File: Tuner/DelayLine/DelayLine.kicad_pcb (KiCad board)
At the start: 2 copper layers, 100 x 100 mm, 87 parts, among them J1 Conn_Coaxial, J10 Conn_Coaxial, J11 Conn_Coaxial, J12 Conn_Coaxial, J13 Conn_01x01, J14 Conn_01x01, J15 Conn_01x01, J16 Conn_01x01, J17 Conn_02x10_Odd_Even, J18 Conn_Coaxial, J19 Conn_Coaxial, J2 Conn_01x01, J20 Conn_Coaxial, J21 Conn_Coaxial, J22 Conn_Coaxial, J23 Conn_Coaxial, J24 Conn_01x01, J25 Conn_01x01, J26 Conn_01x01, J27 Conn_01x01, J28 Conn_01x01, J29 Conn_Coaxial, J3 Conn_Coaxial, J31 Conn_Coaxial, J32 Conn_01x01, J33 Conn_01x01, J34 Conn_01x01, J35 Conn_01x01, J5 Conn_Coaxial, J6 Conn_Coaxial, J7 Conn_Coaxial, J8 Conn_01x02, J9 Conn_01x02

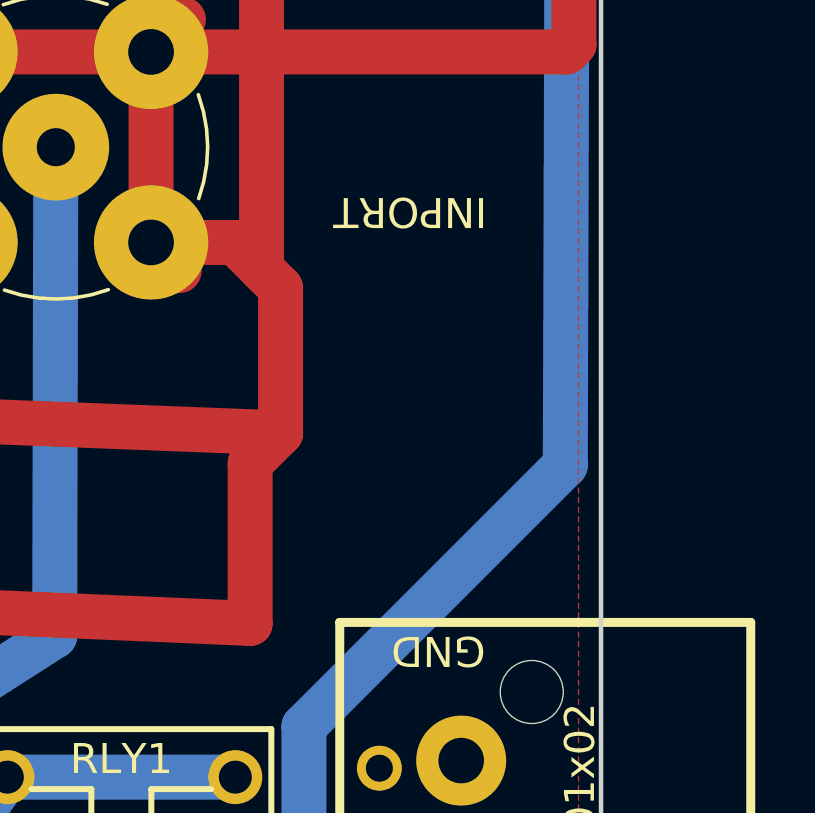
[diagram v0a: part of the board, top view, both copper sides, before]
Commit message: Changed over yet more to BNC
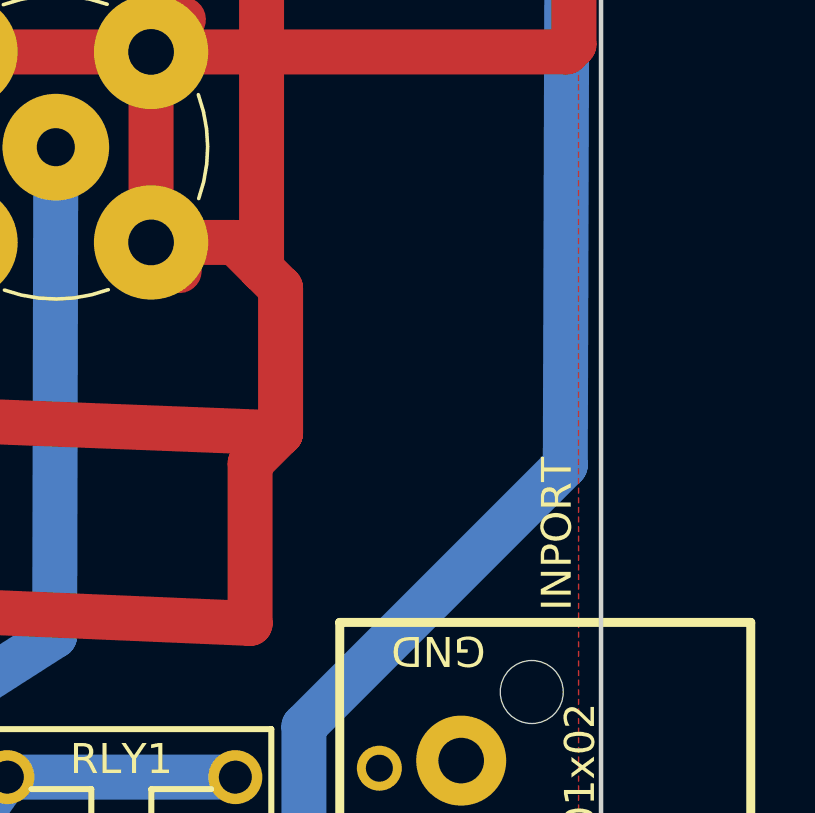
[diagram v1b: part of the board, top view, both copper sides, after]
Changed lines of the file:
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@@
     (links 227)
     (no_connects 0)
-    (area 49.924999 49.924999 150.075001 150.075001)
+    (area 44.941618 47.69538 155.4408 151.075)
     (thickness 1.6)
     (drawings 35)
@@
   )
   (setup
-    (last_trace_width 1.5)
+    (last_trace_width 0.25)
     (user_trace_width 0.35)
     (user_trace_width 0.5)
@@
     (effects (font (size 1 1) (thickness 0.15)))
   )
-  (gr_text INPORT (at 143.637 108.966 180) (layer F.SilkS)
+  (gr_text INPORT (at 148.52904 119.69496 90) (layer F.SilkS)
     (effects (font (size 1 1) (thickness 0.15)))
   )
@@
   (segment (start 137.8104 132.8852) (end 138.35124 132.8852) (width 1.5) (layer B.Cu) (net 62))
   (segment (start 138.35124 132.8852) (end 140.09624 131.1402) (width 1.5) (layer B.Cu) (net 62))
-  (segment (start 148.9202 81.5848) (end 146.51736 78.92796) (width 1.5) (layer B.Cu) (net 62) (status 800020))
+  (segment (start 148.9202 81.5848) (end 146.51736 78.92796) (width 1.5) (layer B.Cu) (net 62) (status 20))
   (segment (start 148.80844 117.40388) (end 148.9202 81.5848) (width 1.5) (layer B.Cu) (net 62))
   (segment (start 140.09624 126.11608) (end 148.80844 117.40388) (width 1.5) (layer B.Cu) (net 62))

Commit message: A few tweaks
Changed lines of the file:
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@@
   (segment (start 137.8104 67.1144) (end 137.9398 67.1144) (width 1.5) (layer B.Cu) (net 52) (status 30))
   (segment (start 124.9072 137.8128) (end 125.7757 137.8128) (width 1.5) (layer B.Cu) (net 53) (status 30))
-  (segment (start 125.7757 137.8128) (end 128.27 136.017) (width 1.5) (layer B.Cu) (net 53) (status 10))
-  (segment (start 128.27 130.533) (end 130.2104 127.8052) (width 1.5) (layer B.Cu) (net 53) (status 20))
-  (segment (start 128.27 136.017) (end 128.27 130.533) (width 1.5) (layer B.Cu) (net 53))
+  (segment (start 125.7757 137.8128) (end 127.5715 135.89) (width 1.5) (layer B.Cu) (net 53) (status 10))
+  (segment (start 127.5715 130.406) (end 130.2104 127.8052) (width 1.5) (layer B.Cu) (net 53) (status 800020))
+  (segment (start 127.5715 135.89) (end 127.5715 130.406) (width 1.5) (layer B.Cu) (net 53))
   (segment (start 124.9072 137.8128) (end 124.9072 138.1533) (width 1.5) (layer F.Cu) (net 53) (status 30))
   (segment (start 137.8104 127.8052) (end 130.2104 127.8052) (width 1.5) (layer B.Cu) (net 53) (status 30))

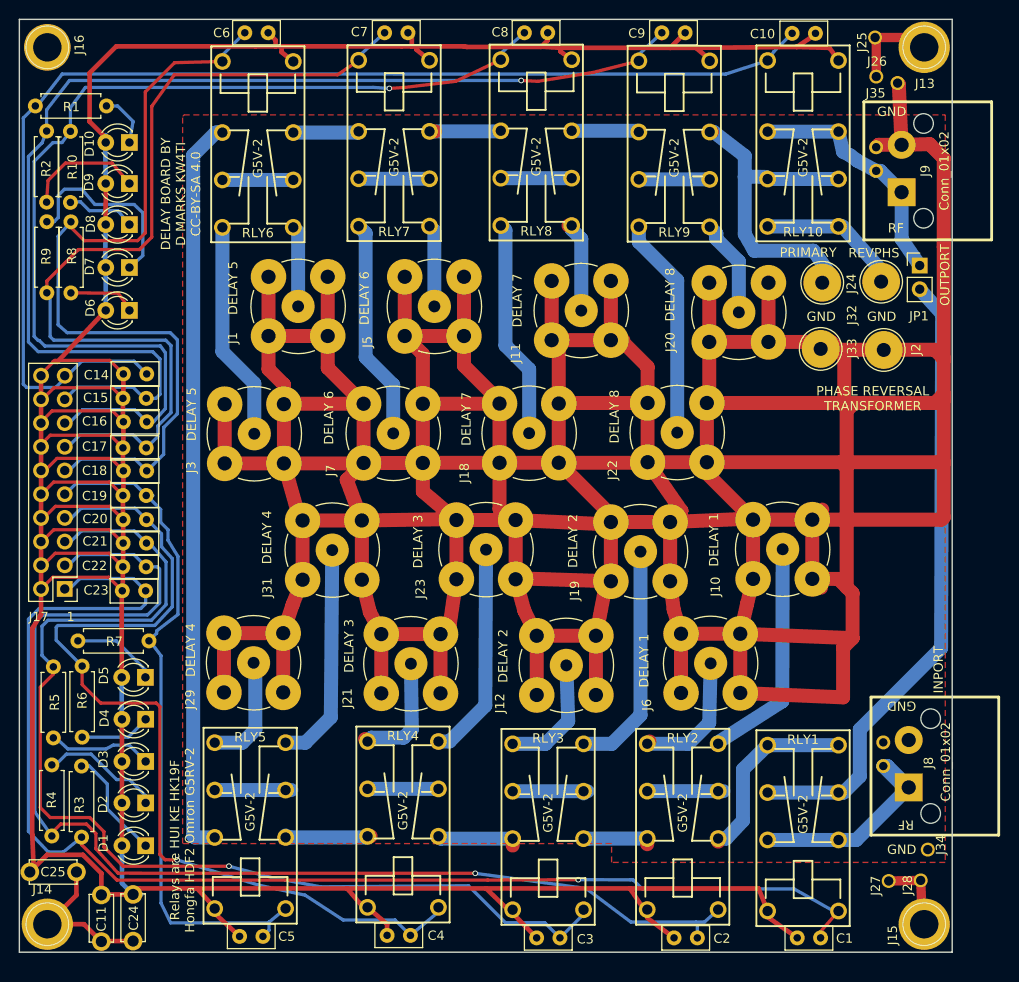
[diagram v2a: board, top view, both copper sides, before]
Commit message: Changed bypass method on delay lines
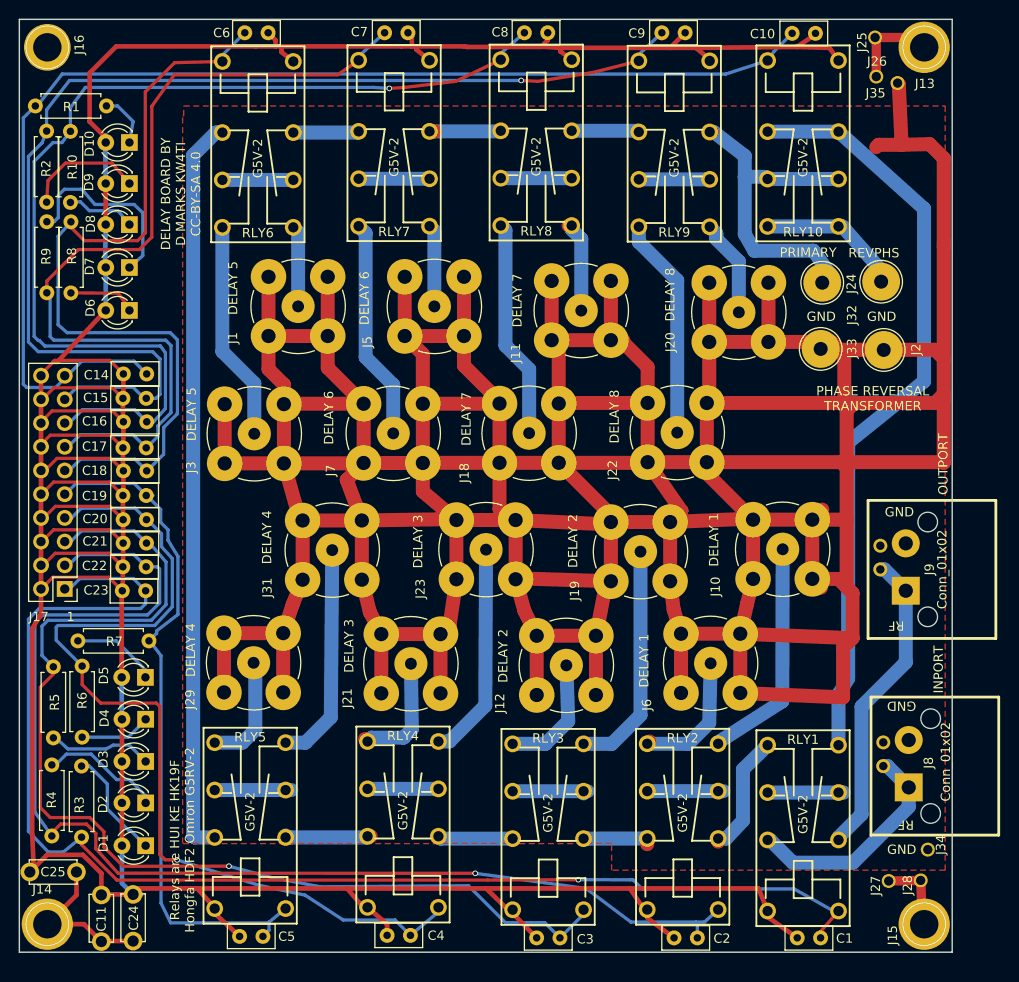
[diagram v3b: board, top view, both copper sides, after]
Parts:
- removed JP1: Jumper_NC_Small, Pin_Headers:Pin_Header_Straight_1x02_Pitch2.54mm
- moved J9 42.7 mm to (154.7, 109.0)
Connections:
- RLY1 pad 6: RFSIG -> RFOUT
- RLY1 pad 8: Net-(RLY1-Pad4) -> RFTHRU
- RLY10 pad 2: RFOUT -> RFTHRU
- RLY10 pad 6: RFOUT -> RFTHRU
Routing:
- net RFTHRU: track 0.00 -> 81.6 mm
- net Net-(RLY1-Pad3): track 67.8 -> 8.70 mm
- net RFGND: track 783.3 -> 766.7 mm
- net Net-(RLY1-Pad4): track 20.6 -> 13.0 mm
- net RFOUT: track 26.1 -> 33.4 mm
- net Net-(RLY3-Pad2): track 8.95 -> 8.21 mm

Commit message: Fixed icom tuning bad tuning report
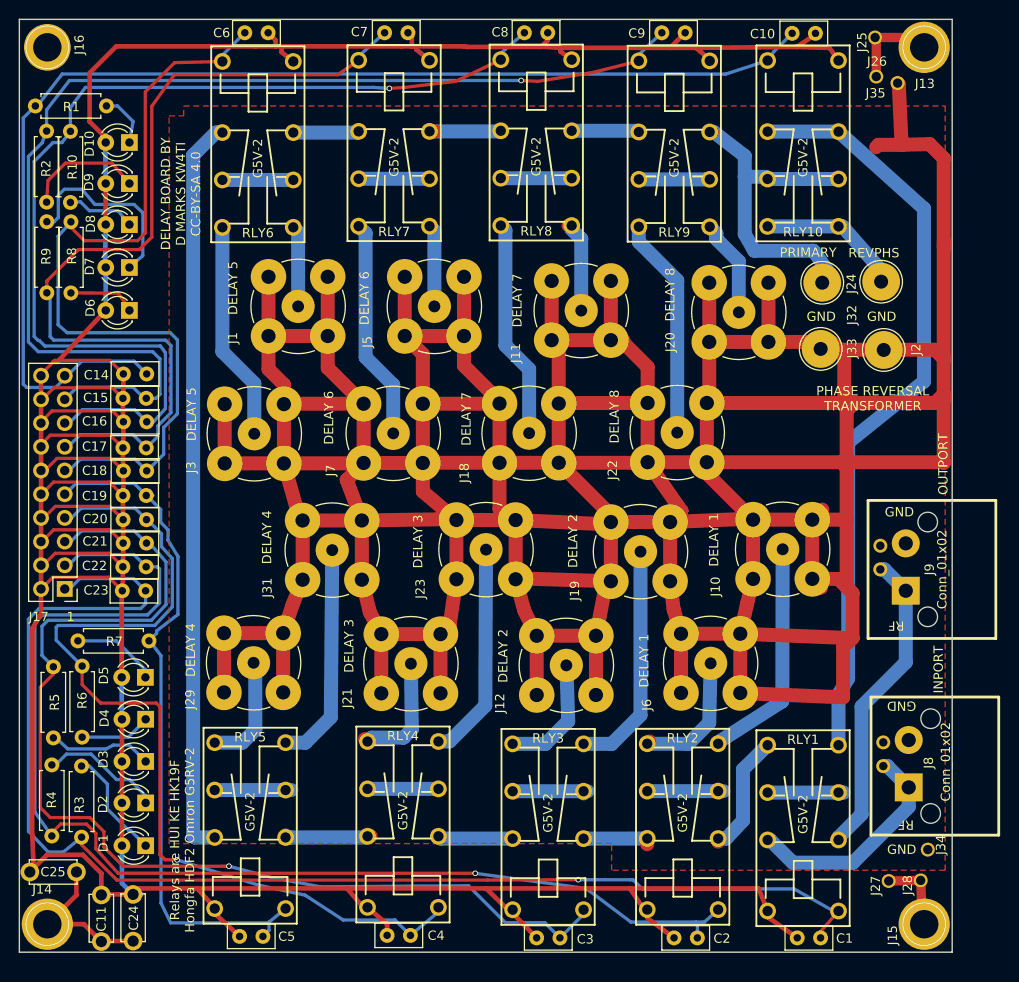
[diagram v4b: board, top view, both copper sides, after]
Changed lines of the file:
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@@
   (segment (start 117.5512 127.4088) (end 117.3072 127.6528) (width 1.5) (layer F.Cu) (net 61) (status 30))
   (segment (start 137.8104 127.8052) (end 137.8104 122.36688) (width 1.5) (layer B.Cu) (net 62))
-  (segment (start 146.97964 70.28924) (end 137.8104 62.0344) (width 1.5) (layer B.Cu) (net 62) (status 800000))
+  (segment (start 146.97964 70.28924) (end 137.8104 62.0344) (width 1.5) (layer B.Cu) (net 62))
   (segment (start 146.97964 88.81364) (end 146.97964 70.28924) (width 1.5) (layer B.Cu) (net 62))
   (segment (start 138.84656 95.36176) (end 146.97964 88.81364) (width 1.5) (layer B.Cu) (net 62))
@@
       (pts
         (xy 67.6148 59.28614) (xy 149.2504 59.28614) (xy 149.2504 141.2113) (xy 113.4872 141.2113) (xy 113.4872 138.3538)
-        (xy 67.5005 138.3538) (xy 67.5005 60.3504) (xy 67.6148 60.3504)
+        (xy 66.0527 138.3538) (xy 66.0527 60.3504) (xy 67.6148 60.3504)
       )
     )

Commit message: Fixed spacing between BNC connectors in Delay Lines
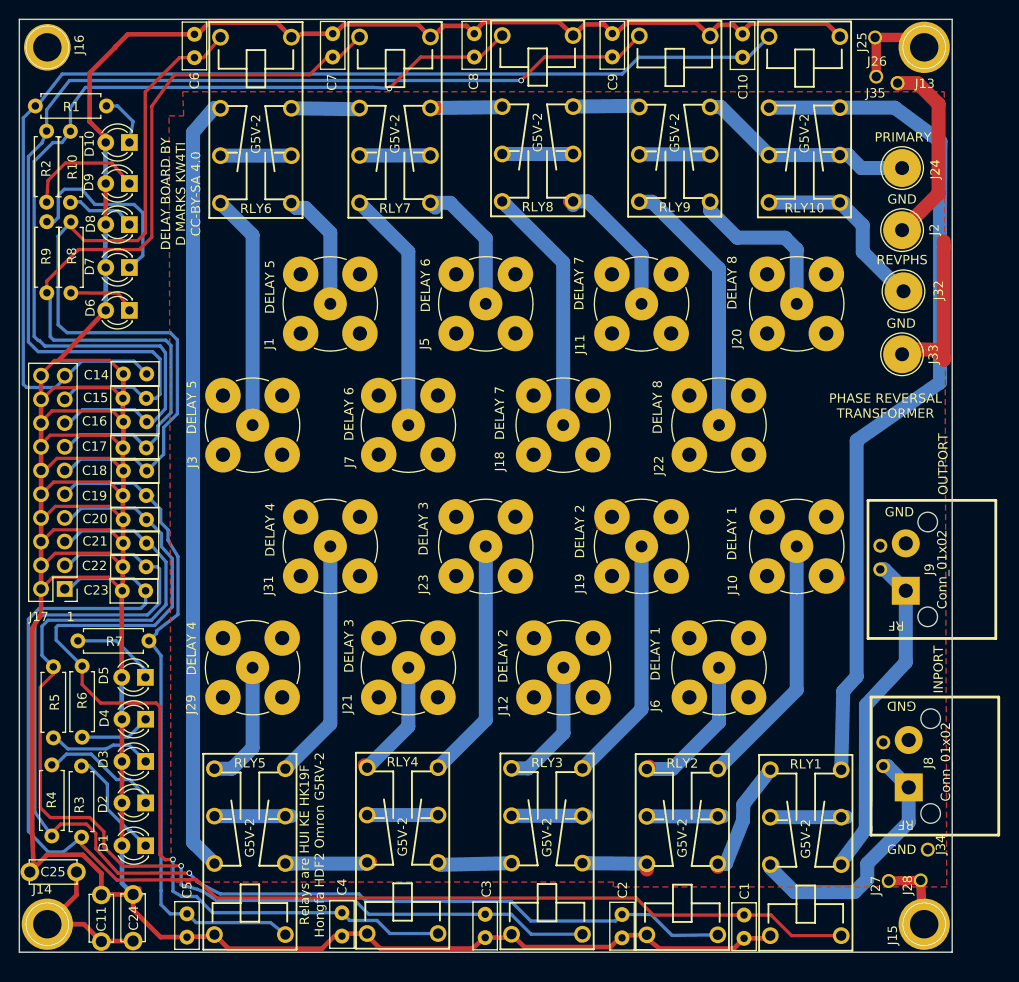
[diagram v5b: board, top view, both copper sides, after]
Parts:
- moved J24 15.0 mm to (144.6, 65.9)
- moved J2 13.0 mm to (144.6, 72.6)
- moved J33 8.75 mm to (144.6, 85.9)
- moved C1 8.56 mm to (127.7, 146.0), turned to 270 degrees
- moved C5 8.49 mm to (68.0, 145.9), turned to 270 degrees
- moved C2 8.46 mm to (114.6, 146.0), turned to 270 degrees
- moved C3 8.40 mm to (99.9, 145.9), turned to 270 degrees
- moved C4 7.73 mm to (84.6, 145.8), turned to 270 degrees
- moved J11 6.50 mm to (116.7, 80.5)
- moved J20 6.27 mm to (133.3, 80.5)
- moved C7 6.14 mm to (83.6, 54.0), turned to 90 degrees
- moved C6 6.02 mm to (68.8, 54.1), turned to 90 degrees
- moved C8 5.97 mm to (98.8, 54.0), turned to 90 degrees
- moved C10 5.91 mm to (127.5, 54.1), turned to 90 degrees
- moved C9 5.91 mm to (113.6, 54.0), turned to 90 degrees
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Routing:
- net RFGND: track 766.7 -> 57.8 mm
- net +5V: track 469.9 -> 436.0 mm
- net Net-(J24-Pad1): track 36.3 -> 24.4 mm
- net RFTHRU: track 81.6 -> 92.2 mm
- net Net-(J20-Pad1): track 10.5 -> 17.8 mm
- net Net-(J5-Pad1): track 8.82 -> 15.8 mm
- net Net-(J11-Pad1): track 9.88 -> 15.7 mm
- net Net-(J1-Pad1): track 8.69 -> 13.9 mm
- net Net-(J22-Pad1): track 23.8 -> 28.3 mm
- net Net-(J32-Pad1): track 16.0 -> 20.5 mm
- net Net-(RLY5-Pad2): track 79.9 -> 83.9 mm
- net Net-(J18-Pad1): track 23.5 -> 27.4 mm
- net RFSIG: track 24.8 -> 28.5 mm
- net Net-(J10-Pad1): track 24.6 -> 27.5 mm
- net Net-(J23-Pad1): track 23.3 -> 25.8 mm
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
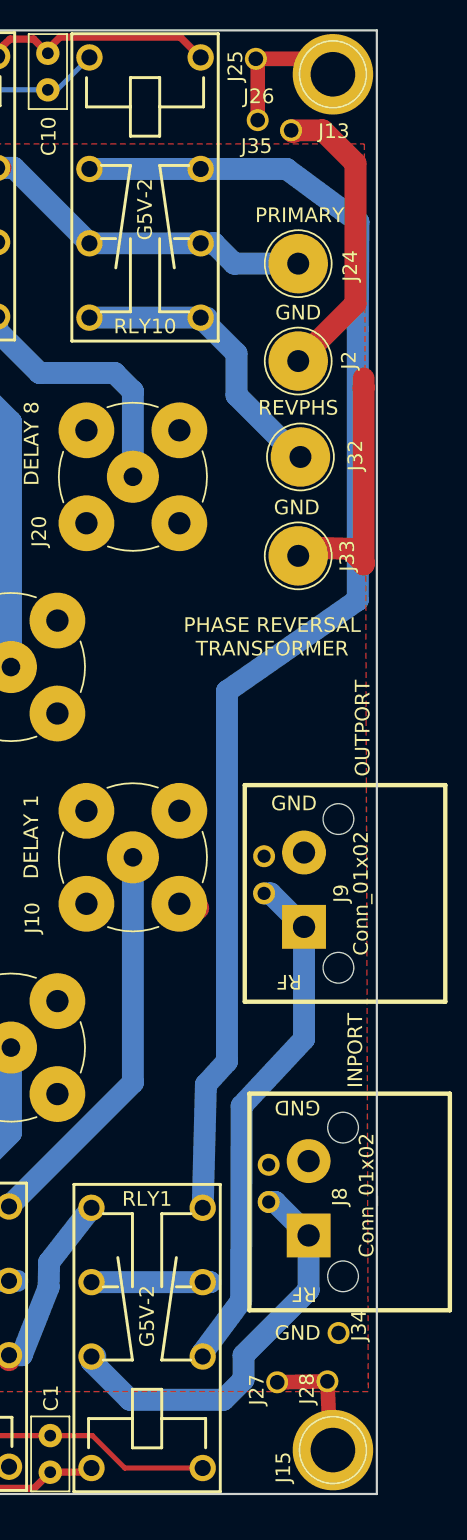
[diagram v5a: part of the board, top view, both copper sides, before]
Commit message: Added extra capacitors between relay power and ground posts
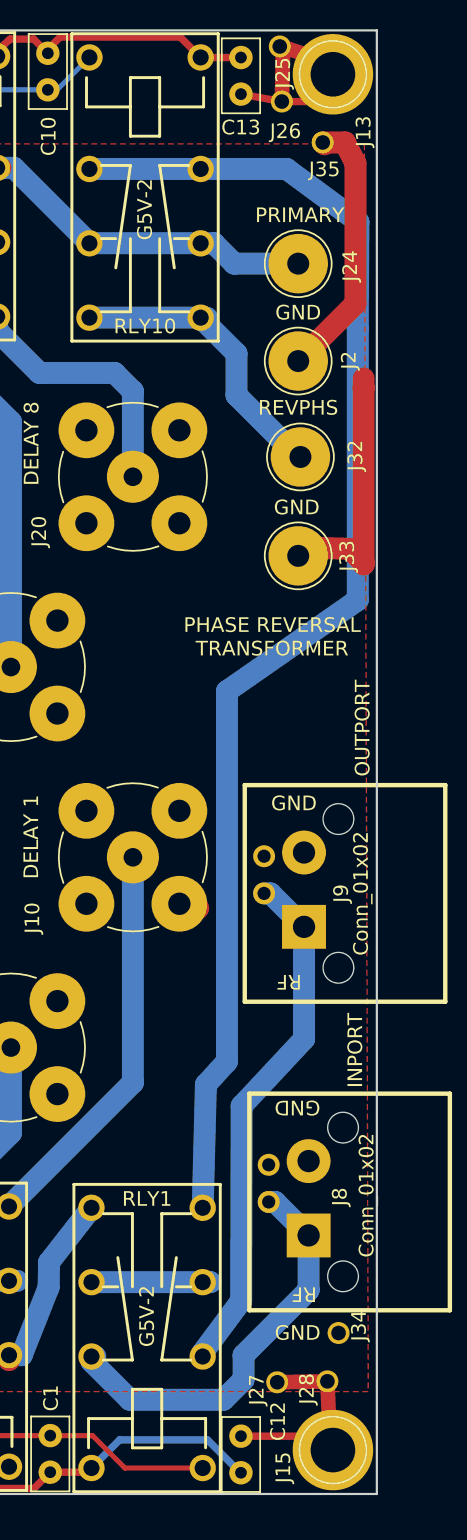
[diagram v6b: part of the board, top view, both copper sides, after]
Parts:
- added C12: 10 nF, Capacitors_THT:C_Disc_D5.0mm_W2.5mm_P2.50mm, F.Cu at (140.7, 146.1)
- added C13: 10 nF, Capacitors_THT:C_Disc_D5.0mm_W2.5mm_P2.50mm, F.Cu at (140.7, 54.4)
- moved J35 2.31 mm to (147.6, 57.7)
- moved J26 2.08 mm to (142.2, 54.9)
- moved J25 1.84 mm to (142.1, 51.1)
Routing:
- net +5V: track 436.0 -> 450.7 mm
- net Net-(C12-Pad1): track 8.21 -> 14.9 mm
- net Net-(C13-Pad1): track 12.6 -> 17.7 mm
- net RFGND: track 57.8 -> 55.6 mm
